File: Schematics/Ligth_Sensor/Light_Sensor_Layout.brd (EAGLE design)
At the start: 39 x 40.6 mm, 7 parts, among them J1 RJ45

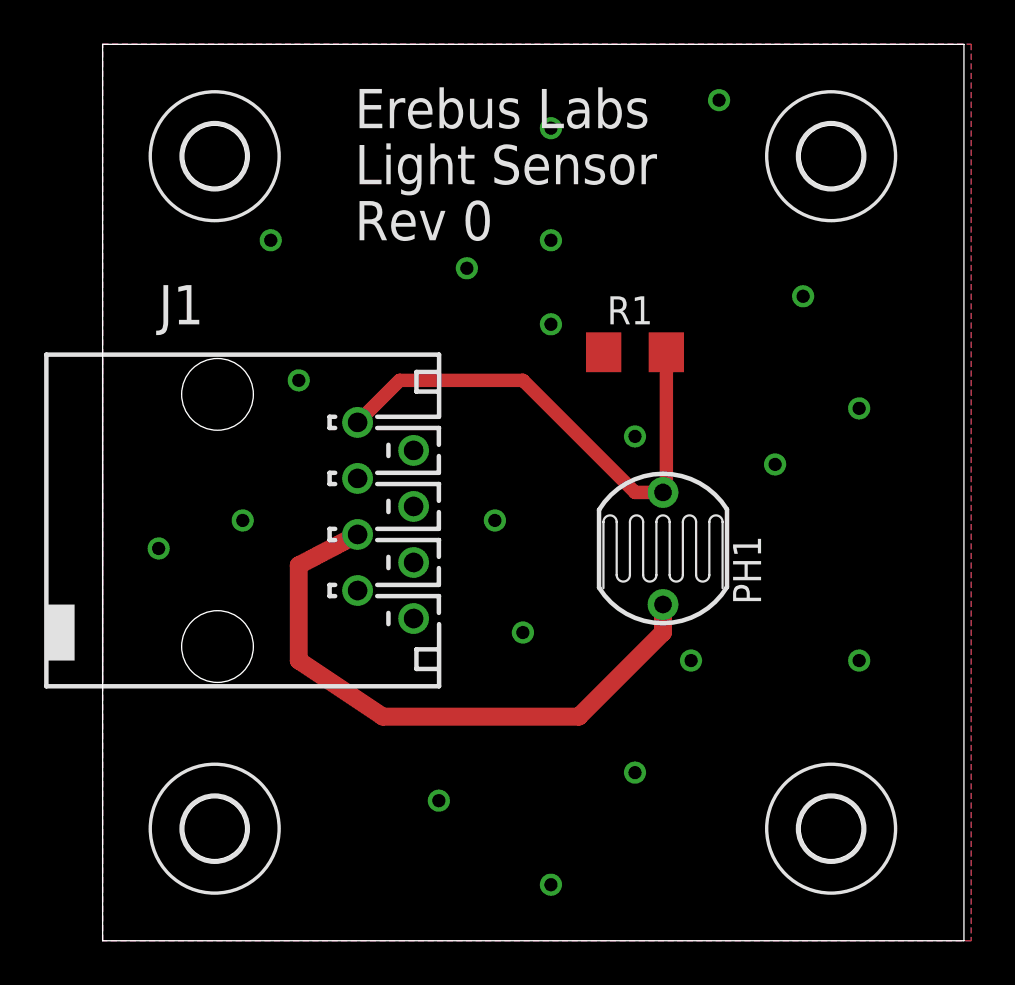
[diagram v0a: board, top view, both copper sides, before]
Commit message: Updated Sensor Module PCBs
Switched Ethernet I/O. Rerouted PCB
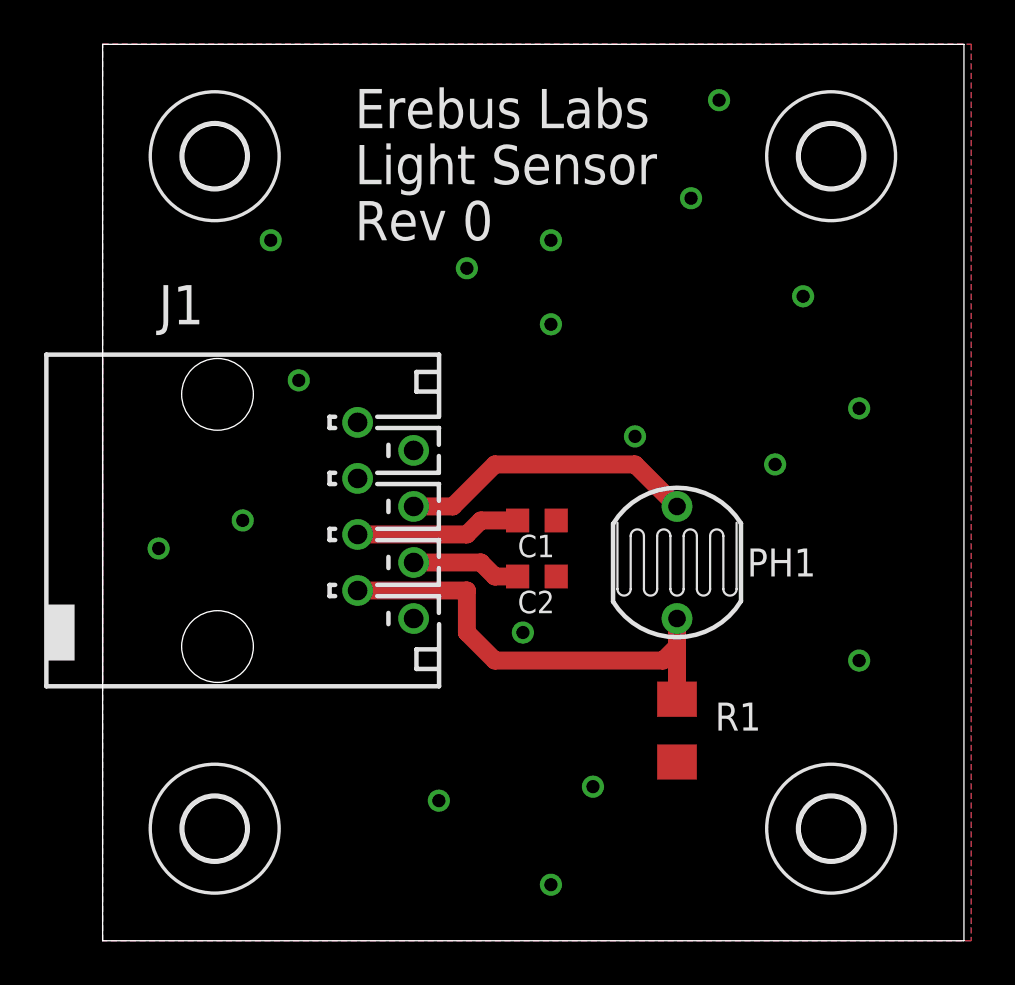
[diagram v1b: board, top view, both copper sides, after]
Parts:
- added C1, C2: (no value), rcl:C0603K
- moved R1 17.3 mm to (26.0, 48.9), turned to 90 degrees
- moved PH1 0.90 mm to (26.0, 56.5), turned to 270 degrees
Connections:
- new net N$23: C1.2, J1.5
- new net N$24: C2.2, J1.6
- net AGND: now also C1.1, C2.1, J1.1; no longer J1.4, J1.6, J1.7
- net N$1: now also J1.4; no longer J1.5
- net N$2: now also J1.7; no longer J1.1
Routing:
- net N$1: track 27.5 -> 13.5 mm
- net N$23: track 0.00 -> 7.52 mm
- net N$24: track 0.00 -> 4.98 mm
- net N$2: track 23.2 -> 20.8 mm
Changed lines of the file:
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@@
 <?xml version="1.0" encoding="utf-8"?>
 <!DOCTYPE eagle SYSTEM "eagle.dtd">
-<eagle version="6.4">
+<eagle version="6.3">
 <drawing>
 <settings>
@@
 <setting verticaltext="up"/>
 </settings>
-<grid distance="0.05" unitdist="inch" unit="inch" style="lines" multiple="1" display="no" altdistance="0.025" altunitdist="inch" altunit="inch"/>
+<grid distance="0.025" unitdist="inch" unit="inch" style="lines" multiple="1" display="no" altdistance="0.025" altunitdist="inch" altunit="inch"/>
 <layers>
 <layer number="1" name="Top" color="4" fill="1" visible="yes" active="yes"/>
@@
 </autorouter>
 <elements>
-<element name="PH1" library="photo-elements" package="VT800" value="VT83N2" x="25.4" y="57.15" rot="R90"/>
-<element name="R1" library="rcl" package="R1206" value="10k" x="24.13" y="66.04"/>
+<element name="PH1" library="photo-elements" package="VT800" value="VT83N2" x="26.035" y="56.515" smashed="yes" rot="R270">
+<attribute name="NAME" x="29.21" y="55.88" size="1.27" layer="25"/>
+<attribute name="VALUE" x="29.21" y="53.975" size="1.27" layer="27"/>
+</element>
+<element name="R1" library="rcl" package="R1206" value="10k" x="26.035" y="48.895" smashed="yes" rot="R90">
+<attribute name="NAME" x="29.845" y="50.165" size="1.27" layer="25" rot="R180"/>
+<attribute name="VALUE" x="29.845" y="48.26" size="1.27" layer="27" rot="R180"/>
+</element>
 <element name="J1" library="con-amp" package="555167-1" value="RJ45" x="6.35" y="58.42" rot="R270"/>
 <element name="H1" library="holes" package="2,8" value="MOUNT-HOLE2.8" x="5.08" y="44.45"/>
@@
 <element name="H3" library="holes" package="2,8" value="MOUNT-HOLE2.8" x="33.02" y="74.93"/>
 <element name="H4" library="holes" package="2,8" value="MOUNT-HOLE2.8" x="5.08" y="74.93"/>
+<element name="C1" library="rcl" package="C0603K" value="" x="19.685" y="58.42" rot="R180"/>
+<element name="C2" library="rcl" package="C0603K" value="" x="19.685" y="55.88" rot="R180"/>
 </elements>
 <signals>
 <signal name="N$1">
-<contactref element="J1" pad="5"/>
 <contactref element="PH1" pad="1"/>
-<wire x1="25.4" y1="54.61" x2="25.4" y2="53.34" width="0.8128" layer="1"/>
-<wire x1="25.4" y1="53.34" x2="21.59" y2="49.53" width="0.8128" layer="1"/>
-<wire x1="21.59" y1="49.53" x2="12.7" y2="49.53" width="0.8128" layer="1"/>
-<wire x1="12.7" y1="49.53" x2="8.89" y2="52.07" width="0.8128" layer="1"/>
-<wire x1="8.89" y1="52.07" x2="8.89" y2="56.388" width="0.8128" layer="1"/>
-<wire x1="8.89" y1="56.388" x2="11.557" y2="57.785" width="0.8128" layer="1"/>
+<contactref element="J1" pad="4"/>
+<wire x1="14.097" y1="59.055" x2="15.875" y2="59.055" width="0.8128" layer="1"/>
+<wire x1="15.875" y1="59.055" x2="17.78" y2="60.96" width="0.8128" layer="1"/>
+<wire x1="17.78" y1="60.96" x2="24.13" y2="60.96" width="0.8128" layer="1"/>
+<wire x1="24.13" y1="60.96" x2="26.035" y2="59.055" width="0.8128" layer="1"/>
 </signal>
 <signal name="N$2">
 <contactref element="PH1" pad="2"/>
 <contactref element="R1" pad="2"/>
-<contactref element="J1" pad="1"/>
-<wire x1="25.4" y1="59.69" x2="25.552" y2="59.69" width="0.6096" layer="1"/>
-<wire x1="25.552" y1="59.69" x2="25.552" y2="66.04" width="0.6096" layer="1"/>
-<wire x1="25.4" y1="59.69" x2="24.13" y2="59.69" width="0.6096" layer="1"/>
-<wire x1="24.13" y1="59.69" x2="19.05" y2="64.77" width="0.6096" layer="1"/>
-<wire x1="19.05" y1="64.77" x2="13.462" y2="64.77" width="0.6096" layer="1"/>
-<wire x1="13.462" y1="64.77" x2="11.557" y2="62.865" width="0.6096" layer="1"/>
+<contactref element="J1" pad="7"/>
+<wire x1="11.557" y1="55.245" x2="16.51" y2="55.245" width="0.8128" layer="1"/>
+<wire x1="26.035" y1="53.975" x2="26.035" y2="52.705" width="0.8128" layer="1"/>
+<wire x1="26.035" y1="52.705" x2="26.035" y2="50.317" width="0.8128" layer="1"/>
+<wire x1="26.035" y1="52.705" x2="25.4" y2="52.07" width="0.8128" layer="1"/>
+<wire x1="25.4" y1="52.07" x2="17.78" y2="52.07" width="0.8128" layer="1"/>
+<wire x1="17.78" y1="52.07" x2="16.51" y2="53.34" width="0.8128" layer="1"/>
+<wire x1="16.51" y1="53.34" x2="16.51" y2="55.245" width="0.8128" layer="1"/>
 </signal>
 <signal name="AGND">
 <contactref element="R1" pad="1"/>
-<contactref element="J1" pad="2"/>
-<contactref element="J1" pad="3"/>
-<contactref element="J1" pad="4"/>
-<contactref element="J1" pad="6"/>
-<contactref element="J1" pad="7"/>
-<contactref element="J1" pad="8"/>
 <polygon width="0.4064" layer="16">
 <vertex x="0" y="80.01"/>
@@
 <vertex x="0" y="39.37"/>
 </polygon>
-</signal>
-<signal name="N$3">
+<contactref element="J1" pad="8"/>
+<contactref element="J1" pad="1"/>
+<contactref element="J1" pad="2"/>
+<contactref element="J1" pad="3"/>
+<contactref element="C1" pad="1"/>
+<contactref element="C2" pad="1"/>
+<via x="20.32" y="41.91" extent="1-16" drill="0.6" diameter="0.4064"/>
+<via x="15.24" y="45.72" extent="1-16" drill="0.6" diameter="0.4064"/>
+<via x="22.225" y="46.355" extent="1-16" drill="0.6" diameter="0.4064"/>
+<via x="34.29" y="52.07" extent="1-16" drill="0.6" diameter="0.4064"/>
+<via x="34.29" y="63.5" extent="1-16" drill="0.6" diameter="0.4064"/>
+<via x="30.48" y="60.96" extent="1-16" drill="0.6" diameter="0.4064"/>
+<via x="24.13" y="62.23" extent="1-16" drill="0.6" diameter="0.4064"/>
+<via x="19.05" y="53.34" extent="1-16" drill="0.6" diameter="0.4064"/>
+<via x="31.75" y="68.58" extent="1-16" drill="0.6" diameter="0.4064"/>
+<via x="20.32" y="67.31" extent="1-16" drill="0.6" diameter="0.4064"/>
+<via x="6.35" y="58.42" extent="1-16" drill="0.6" diameter="0.4064"/>
+<via x="2.54" y="57.15" extent="1-16" drill="0.6" diameter="0.4064"/>
+<via x="8.89" y="64.77" extent="1-16" drill="0.6" diameter="0.4064"/>
 <via x="7.62" y="71.12" extent="1-16" drill="0.6" diameter="0.4064"/>
-</signal>
-<signal name="N$4">
 <via x="16.51" y="69.85" extent="1-16" drill="0.6" diameter="0.4064"/>
-</signal>
-<signal name="N$5">
 <via x="20.32" y="71.12" extent="1-16" drill="0.6" diameter="0.4064"/>
-</signal>
-<signal name="N$6">
 <via x="27.94" y="77.47" extent="1-16" drill="0.6" diameter="0.4064"/>
-</signal>
-<signal name="N$7">
-<via x="31.75" y="68.58" extent="1-16" drill="0.6" diameter="0.4064"/>
-</signal>
-<signal name="N$8">
-<via x="24.13" y="62.23" extent="1-16" drill="0.6" diameter="0.4064"/>
-</signal>
-<signal name="N$9">
-<via x="20.32" y="67.31" extent="1-16" drill="0.6" diameter="0.4064"/>
-</signal>
-<signal name="N$10">
-<via x="8.89" y="64.77" extent="1-16" drill="0.6" diameter="0.4064"/>
-</signal>
-<signal name="N$11">
-<via x="24.13" y="46.99" extent="1-16" drill="0.6" diameter="0.4064"/>
-</signal>
-<signal name="N$12">
-<via x="2.54" y="57.15" extent="1-16" drill="0.6" diameter="0.4064"/>
-</signal>
-<signal name="N$13">
-<via x="6.35" y="58.42" extent="1-16" drill="0.6" diameter="0.4064"/>
-</signal>
-<signal name="N$14">
-<via x="17.78" y="58.42" extent="1-16" drill="0.6" diameter="0.4064"/>
-</signal>
-<signal name="N$15">
-<via x="19.05" y="53.34" extent="1-16" drill="0.6" diameter="0.4064"/>
+<via x="26.67" y="73.025" extent="1-16" drill="0.6" diameter="0.4064"/>
+<wire x1="20.32" y1="71.12" x2="26.67" y2="73.025" width="0" layer="19" extent="1-1"/>
 </signal>
 <signal name="N$16">
-<via x="26.67" y="52.07" extent="1-16" drill="0.6" diameter="0.4064"/>
-</signal>
-<signal name="N$17">
-<via x="30.48" y="60.96" extent="1-16" drill="0.6" diameter="0.4064"/>
-</signal>
-<signal name="N$18">
-<via x="34.29" y="63.5" extent="1-16" drill="0.6" diameter="0.4064"/>
-</signal>
-<signal name="N$19">
-<via x="34.29" y="52.07" extent="1-16" drill="0.6" diameter="0.4064"/>
-</signal>
-<signal name="N$20">
-<via x="20.32" y="41.91" extent="1-16" drill="0.6" diameter="0.4064"/>
-</signal>
-<signal name="N$21">
-<via x="15.24" y="45.72" extent="1-16" drill="0.6" diameter="0.4064"/>
-</signal>
-<signal name="N$22">
-<via x="20.32" y="76.2" extent="1-16" drill="0.6" diameter="0.4064"/>
+</signal>
+<signal name="N$23">
+<contactref element="J1" pad="5"/>
+<contactref element="C1" pad="2"/>
+<wire x1="11.557" y1="57.785" x2="16.51" y2="57.785" width="0.8128" layer="1"/>
+<wire x1="16.51" y1="57.785" x2="17.145" y2="58.42" width="0.8128" layer="1"/>
+<wire x1="17.145" y1="58.42" x2="18.81" y2="58.42" width="0.8128" layer="1"/>
+</signal>
+<signal name="N$24">
+<contactref element="J1" pad="6"/>
+<contactref element="C2" pad="2"/>
+<wire x1="14.097" y1="56.515" x2="17.145" y2="56.515" width="0.8128" layer="1"/>
+<wire x1="17.145" y1="56.515" x2="17.78" y2="55.88" width="0.8128" layer="1"/>
+<wire x1="17.78" y1="55.88" x2="18.81" y2="55.88" width="0.8128" layer="1"/>
 </signal>
 </signals>

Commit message: Layout for final inspection
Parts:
- C1, C2: value (none) -> 0.1uF
- PH1: value VT83N2 -> VT90N2; device photo-elements:VT800 -> photo-elements:VT900
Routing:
- net N$2: track 20.8 -> 22.1 mm
- net N$1: track 13.5 -> 14.5 mm
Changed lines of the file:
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@@
 <?xml version="1.0" encoding="utf-8"?>
 <!DOCTYPE eagle SYSTEM "eagle.dtd">
-<eagle version="6.3">
+<eagle version="6.4">
 <drawing>
 <settings>
@@
 <layer number="25" name="tNames" color="7" fill="1" visible="yes" active="yes"/>
 <layer number="26" name="bNames" color="7" fill="1" visible="yes" active="yes"/>
-<layer number="27" name="tValues" color="7" fill="1" visible="yes" active="yes"/>
+<layer number="27" name="tValues" color="7" fill="1" visible="no" active="yes"/>
 <layer number="28" name="bValues" color="7" fill="1" visible="yes" active="yes"/>
 <layer number="29" name="tStop" color="7" fill="3" visible="no" active="yes"/>
@@
 </class>
 </classes>
-<designrules name="default">
+<designrules name="LaenPCBOrder">
 <description language="de">&lt;b&gt;EAGLE Design Rules&lt;/b&gt;
 &lt;p&gt;
@@
 Einstellungen hier und speichern die Design Rules unter
 einem neuen Namen ab.</description>
-<description language="en">&lt;b&gt;EAGLE Design Rules&lt;/b&gt;
+<description language="en">&lt;b&gt;Laen's PCB Order Design Rules&lt;/b&gt;
 &lt;p&gt;
-The default Design Rules have been set to cover
-a wide range of applications. Your particular design
-may have different requirements, so please make the
-necessary adjustments and save your customized
-design rules under a new name.</description>
+Please make sure your boards conform to these design rules.</description>
 <param name="layerSetup" value="(1*16)"/>
-<param name="mtCopper" value="0.035mm 0.035mm 0.035mm 0.035mm 0.035mm 0.035mm 0.035mm 0.035mm 0.035mm 0.035mm 0.035mm 0.035mm 0.035mm 0.035mm 0.035mm 0.035mm"/>
-<param name="mtIsolate" value="1.5mm 0.15mm 0.2mm 0.15mm 0.2mm 0.15mm 0.2mm 0.15mm 0.2mm 0.15mm 0.2mm 0.15mm 0.2mm 0.15mm 0.2mm"/>
-<param name="mdWireWire" value="8mil"/>
-<param name="mdWirePad" value="8mil"/>
-<param name="mdWireVia" value="8mil"/>
-<param name="mdPadPad" value="8mil"/>
-<param name="mdPadVia" value="8mil"/>
-<param name="mdViaVia" value="8mil"/>
-<param name="mdSmdPad" value="8mil"/>
-<param name="mdSmdVia" value="8mil"/>
-<param name="mdSmdSmd" value="8mil"/>
+<param name="mtCopper" value="0.0356mm 0.0356mm 0.0356mm 0.0356mm 0.0356mm 0.0356mm 0.0356mm 0.0356mm 0.0356mm 0.0356mm 0.0356mm 0.0356mm 0.0356mm 0.0356mm 0.0356mm 0.0356mm"/>
+<param name="mtIsolate" value="1.5011mm 0.1499mm 0.2007mm 0.1499mm 0.2007mm 0.1499mm 0.2007mm 0.1499mm 0.2007mm 0.1499mm 0.2007mm 0.1499mm 0.2007mm 0.1499mm 0.2007mm"/>
+<param name="mdWireWire" value="6mil"/>
+<param name="mdWirePad" value="6mil"/>
+<param name="mdWireVia" value="6mil"/>
+<param name="mdPadPad" value="6mil"/>
+<param name="mdPadVia" value="6mil"/>
+<param name="mdViaVia" value="6mil"/>
+<param name="mdSmdPad" value="6mil"/>
+<param name="mdSmdVia" value="6mil"/>
+<param name="mdSmdSmd" value="6mil"/>
 <param name="mdViaViaSameLayer" value="8mil"/>
 <param name="mnLayersViaInSmd" value="2"/>
-<param name="mdCopperDimension" value="40mil"/>
-<param name="mdDrill" value="8mil"/>
+<param name="mdCopperDimension" value="15mil"/>
+<param name="mdDrill" value="6mil"/>
 <param name="mdSmdStop" value="0mil"/>
-<param name="msWidth" value="10mil"/>
-<param name="msDrill" value="24mil"/>
-<param name="msMicroVia" value="9.99mm"/>
+<param name="msWidth" value="6mil"/>
+<param name="msDrill" value="13mil"/>
+<param name="msMicroVia" value="13mil"/>
 <param name="msBlindViaRatio" value="0.5"/>
 <param name="rvPadTop" value="0.25"/>
@@
 <param name="rvMicroViaOuter" value="0.25"/>
 <param name="rvMicroViaInner" value="0.25"/>
-<param name="rlMinPadTop" value="10mil"/>
+<param name="rlMinPadTop" value="7mil"/>
 <param name="rlMaxPadTop" value="20mil"/>
-<param name="rlMinPadInner" value="10mil"/>
+<param name="rlMinPadInner" value="7mil"/>
 <param name="rlMaxPadInner" value="20mil"/>
-<param name="rlMinPadBottom" value="10mil"/>
+<param name="rlMinPadBottom" value="7mil"/>
 <param name="rlMaxPadBottom" value="20mil"/>
-<param name="rlMinViaOuter" value="8mil"/>
+<param name="rlMinViaOuter" value="7mil"/>
 <param name="rlMaxViaOuter" value="20mil"/>
-<param name="rlMinViaInner" value="8mil"/>
+<param name="rlMinViaInner" value="7mil"/>
 <param name="rlMaxViaInner" value="20mil"/>
 <param name="rlMinMicroViaOuter" value="4mil"/>
@@
 <param name="mvStopFrame" value="1"/>
 <param name="mvCreamFrame" value="0"/>
-<param name="mlMinStopFrame" value="4mil"/>
-<param name="mlMaxStopFrame" value="4mil"/>
+<param name="mlMinStopFrame" value="3mil"/>
+<param name="mlMaxStopFrame" value="3mil"/>
 <param name="mlMinCreamFrame" value="0mil"/>
 <param name="mlMaxCreamFrame" value="0mil"/>
@@
 </autorouter>
 <elements>
-<element name="PH1" library="photo-elements" package="VT800" value="VT83N2" x="26.035" y="56.515" smashed="yes" rot="R270">
+<element name="PH1" library="photo-elements" package="VT900" value="VT90N2" x="26.035" y="56.515" smashed="yes" rot="R270">
 <attribute name="NAME" x="29.21" y="55.88" size="1.27" layer="25"/>
-<attribute name="VALUE" x="29.21" y="53.975" size="1.27" layer="27"/>
 </element>
 <element name="R1" library="rcl" package="R1206" value="10k" x="26.035" y="48.895" smashed="yes" rot="R90">
@@
 <element name="H3" library="holes" package="2,8" value="MOUNT-HOLE2.8" x="33.02" y="74.93"/>
 <element name="H4" library="holes" package="2,8" value="MOUNT-HOLE2.8" x="5.08" y="74.93"/>
-<element name="C1" library="rcl" package="C0603K" value="" x="19.685" y="58.42" rot="R180"/>
-<element name="C2" library="rcl" package="C0603K" value="" x="19.685" y="55.88" rot="R180"/>
+<element name="C1" library="rcl" package="C0603K" value="0.1uF" x="19.685" y="58.42" rot="R180"/>
+<element name="C2" library="rcl" package="C0603K" value="0.1uF" x="19.685" y="55.88" rot="R180"/>
 </elements>
 <signals>
@@
 <wire x1="15.875" y1="59.055" x2="17.78" y2="60.96" width="0.8128" layer="1"/>
 <wire x1="17.78" y1="60.96" x2="24.13" y2="60.96" width="0.8128" layer="1"/>
-<wire x1="24.13" y1="60.96" x2="26.035" y2="59.055" width="0.8128" layer="1"/>
+<wire x1="24.13" y1="60.96" x2="26.035" y2="57.785" width="0.8128" layer="1"/>
 </signal>
 <signal name="N$2">
@@
 <contactref element="J1" pad="7"/>
 <wire x1="11.557" y1="55.245" x2="16.51" y2="55.245" width="0.8128" layer="1"/>
-<wire x1="26.035" y1="53.975" x2="26.035" y2="52.705" width="0.8128" layer="1"/>
+<wire x1="26.035" y1="55.245" x2="26.035" y2="52.705" width="0.8128" layer="1"/>
 <wire x1="26.035" y1="52.705" x2="26.035" y2="50.317" width="0.8128" layer="1"/>
 <wire x1="26.035" y1="52.705" x2="25.4" y2="52.07" width="0.8128" layer="1"/>
@@
 <via x="27.94" y="77.47" extent="1-16" drill="0.6" diameter="0.4064"/>
 <via x="26.67" y="73.025" extent="1-16" drill="0.6" diameter="0.4064"/>
-<wire x1="20.32" y1="71.12" x2="26.67" y2="73.025" width="0" layer="19" extent="1-1"/>
 </signal>
 <signal name="N$16">
